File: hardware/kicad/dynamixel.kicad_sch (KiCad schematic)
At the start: 0 parts

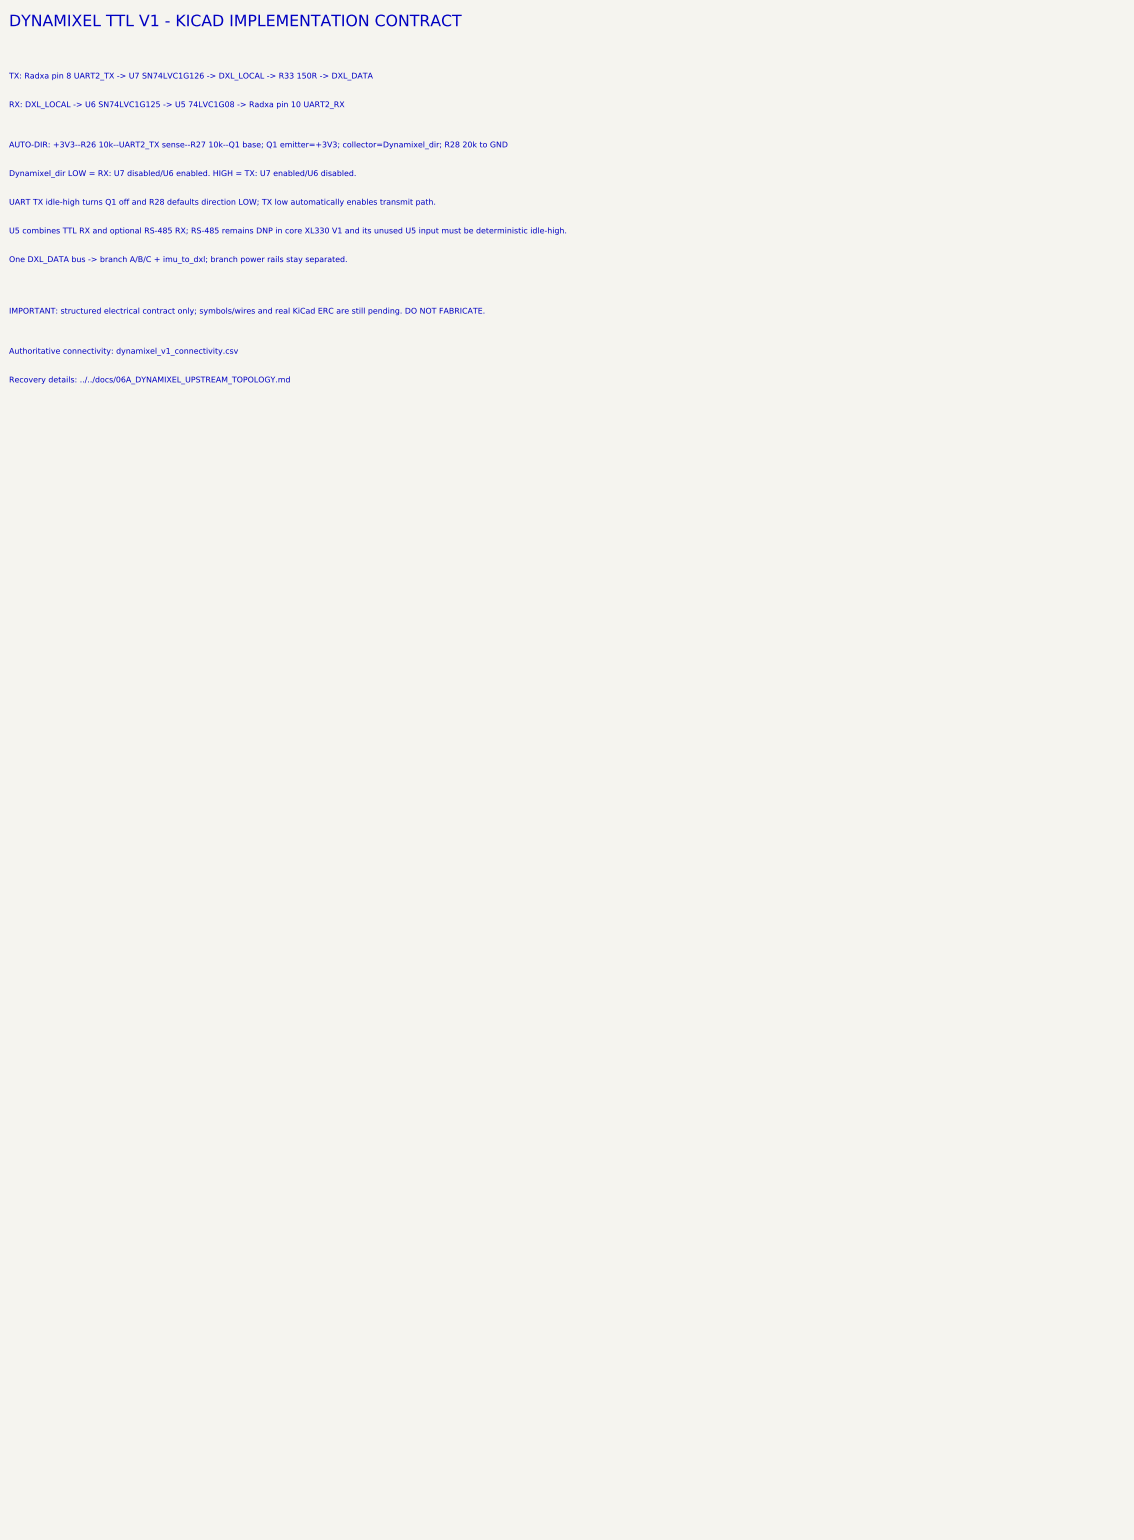
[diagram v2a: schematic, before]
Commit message: [verified] refactor(hardware): restore strict single-board Radxa port
Import the routed upstream Pollen Robot HAT as the active design, adapt the critical host nets for Radxa ZERO 3W, remove the divergent high-current redesign artifacts, and add regenerated baseline-aware KiCad validation.
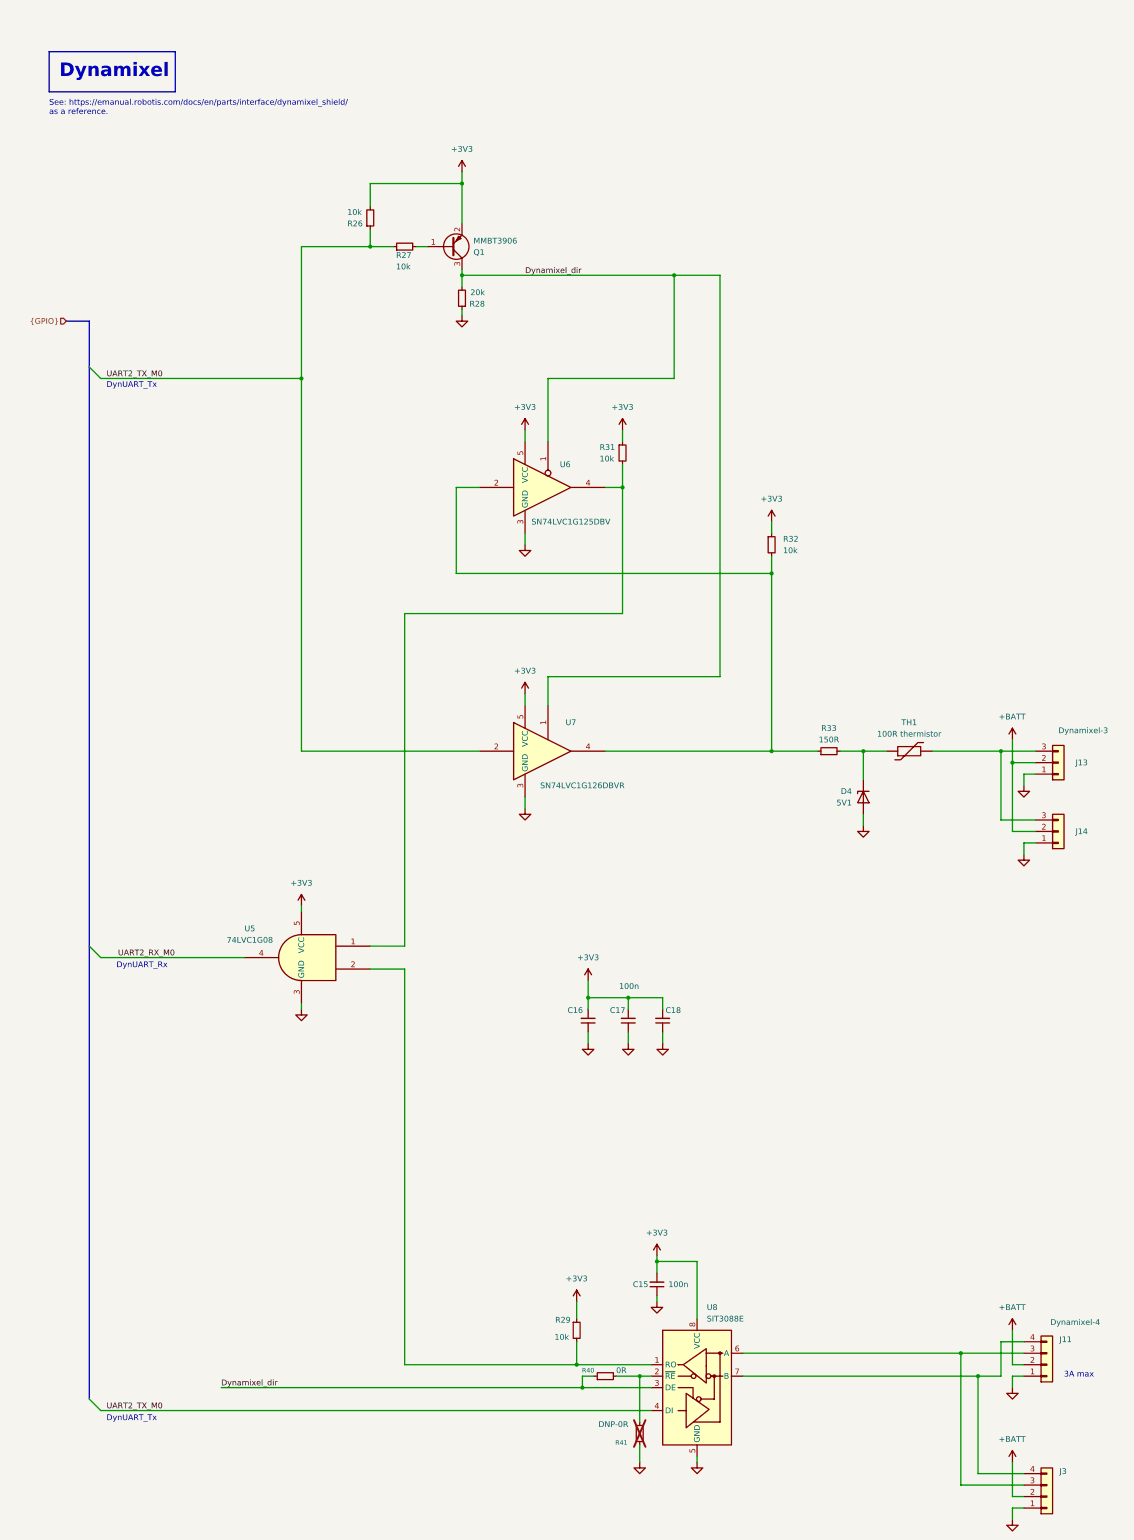
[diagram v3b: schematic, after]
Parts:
- added C15, C16, C17, C18: 100n, Capacitor_SMD:C_0402_1005Metric, symbol Device:C_Small
- added D4: 5V1, Diode_SMD:D_SOD-323, symbol Device:D_Zener
- added J11, J3: Dynamixel-4, Connector_JST:JST_EH_B4B-EH-A_1x04_P2.50mm_Vertical, symbol Connector_Generic:Conn_01x04
- added J13, J14: Dynamixel-3, Connector_JST:JST_EH_B3B-EH-A_1x03_P2.50mm_Vertical, symbol Connector_Generic:Conn_01x03
- added Q1: MMBT3906, Package_TO_SOT_SMD:SOT-23, symbol Transistor_BJT:MMBT3906
- added R26, R27, R29, R31, R32: 10k, Resistor_SMD:R_0402_1005Metric, symbol Device:R_Small
- added R28: 20k, Resistor_SMD:R_0402_1005Metric, symbol Device:R_Small
- added R33: 150R, Resistor_SMD:R_0402_1005Metric, symbol Device:R_Small
- added R40: 0R, Resistor_SMD:R_0402_1005Metric, symbol Device:R_Small
- added R41: DNP-0R, Resistor_SMD:R_0402_1005Metric, symbol Device:R_Small
- added TH1: 100R thermistor, Resistor_SMD:R_0603_1608Metric, symbol Device:Thermistor
- added U5: 74LVC1G08, Package_TO_SOT_SMD:SOT-23-5, symbol 74xGxx:74LVC1G08
- added U6: SN74LVC1G125DBV, Package_TO_SOT_SMD:SOT-23-5, symbol 74xGxx:74LVC1G125
- added U7: SN74LVC1G126DBVR, Package_TO_SOT_SMD:SOT-23-5, symbol 74xGxx:74LVC1G126
- added U8: SIT3088E, Package_SO:MSOP-8-1EP_3x3mm_P0.65mm_EP1.5x1.8mm, symbol Interface_UART:SP3485CN
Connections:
- new net: Q1.1 (B), R27.2
- new net: J13.3 (Pin_3), J14.3 (Pin_3), TH1.2
- new net: R29.2, U5.2, U8.1 (RO)
- new net: R40.2, R41.2, U8.2 (~{RE})
- new net: J11.3 (Pin_3), J3.3 (Pin_3), U8.6 (A)
- new net: J11.4 (Pin_4), J3.4 (Pin_4), U8.7 (B)
- new net: R32.2, R33.1, U6.2, U7.4
- new net: R31.2, U5.1, U6.4
- new net: D4.1 (K), R33.2, TH1.1
- new net +3V3: C15.2, C16.2, C17.2, C18.2, Q1.2 (E), R26.2, R29.1, R31.1, R32.1, U5.5 (VCC), U6.5 (VCC), U7.5 (VCC), U8.8 (VCC)
- new net +BATT: J11.2 (Pin_2), J13.2 (Pin_2), J14.2 (Pin_2), J3.2 (Pin_2)
- new net Dynamixel_dir: Q1.3 (C), R28.2, R40.1, U6.1, U7.1, U8.3 (DE)
- new net GND: C15.1, C16.1, C17.1, C18.1, D4.2 (A), J11.1 (Pin_1), J13.1 (Pin_1), J14.1 (Pin_1), J3.1 (Pin_1), R28.1, R41.1, U5.3 (GND), U6.3 (GND), U7.3 (GND), U8.5 (GND)
- new net UART2_RX_M0: U5.4
- new net UART2_TX_M0: R26.1, R27.1, U7.2, U8.4 (DI)
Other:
- note added: "3A max"
- note added: "DynUART_Rx"
- note added: "DynUART_Tx"
- note added: "See: https://emanual.robotis.com/docs/en/parts/interface/dynamixel_shield/ as a reference."
- note removed: "AUTO-DIR: +3V3--R26 10k--UART2_TX sense--R27 10k--Q1 base; Q1 emitter=+3V3; collector=Dynamixel_dir; R28 20k to GND"
- note removed: "Authoritative connectivity: dynamixel_v1_connectivity.csv"
- note removed: "DYNAMIXEL TTL V1 - KICAD IMPLEMENTATION CONTRACT"
- note removed: "Dynamixel_dir LOW = RX: U7 disabled/U6 enabled. HIGH = TX: U7 enabled/U6 disabled."
- note removed: "IMPORTANT: structured electrical contract only; symbols/wires and real KiCad ERC are still pending. DO NOT FABRICATE."
- note removed: "One DXL_DATA bus -> branch A/B/C + imu_to_dxl; branch power rails stay separated."
- note removed: "RX: DXL_LOCAL -> U6 SN74LVC1G125 -> U5 74LVC1G08 -> Radxa pin 10 UART2_RX"
- note removed: "Recovery details: ../../docs/06A_DYNAMIXEL_UPSTREAM_TOPOLOGY.md"
- note removed: "TX: Radxa pin 8 UART2_TX -> U7 SN74LVC1G126 -> DXL_LOCAL -> R33 150R -> DXL_DATA"
- note removed: "U5 combines TTL RX and optional RS-485 RX; RS-485 remains DNP in core XL330 V1 and its unused U5 input must be deterministic idle-high."
- note removed: "UART TX idle-high turns Q1 off and R28 defaults direction LOW; TX low automatically enables transmit path."
- company: juper007 / DIY -> Pollen Robotics / Hugging Face
- title: Radxa ZERO 3W Robot HAT - Dynamixel TTL V1 -> Radxa ZERO 3W Robot HAT
